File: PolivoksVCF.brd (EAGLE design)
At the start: 39.4 x 97.5 mm, 42 parts, among them IC1 TL072P, IC2 LM4250P, IC3 LM4250P

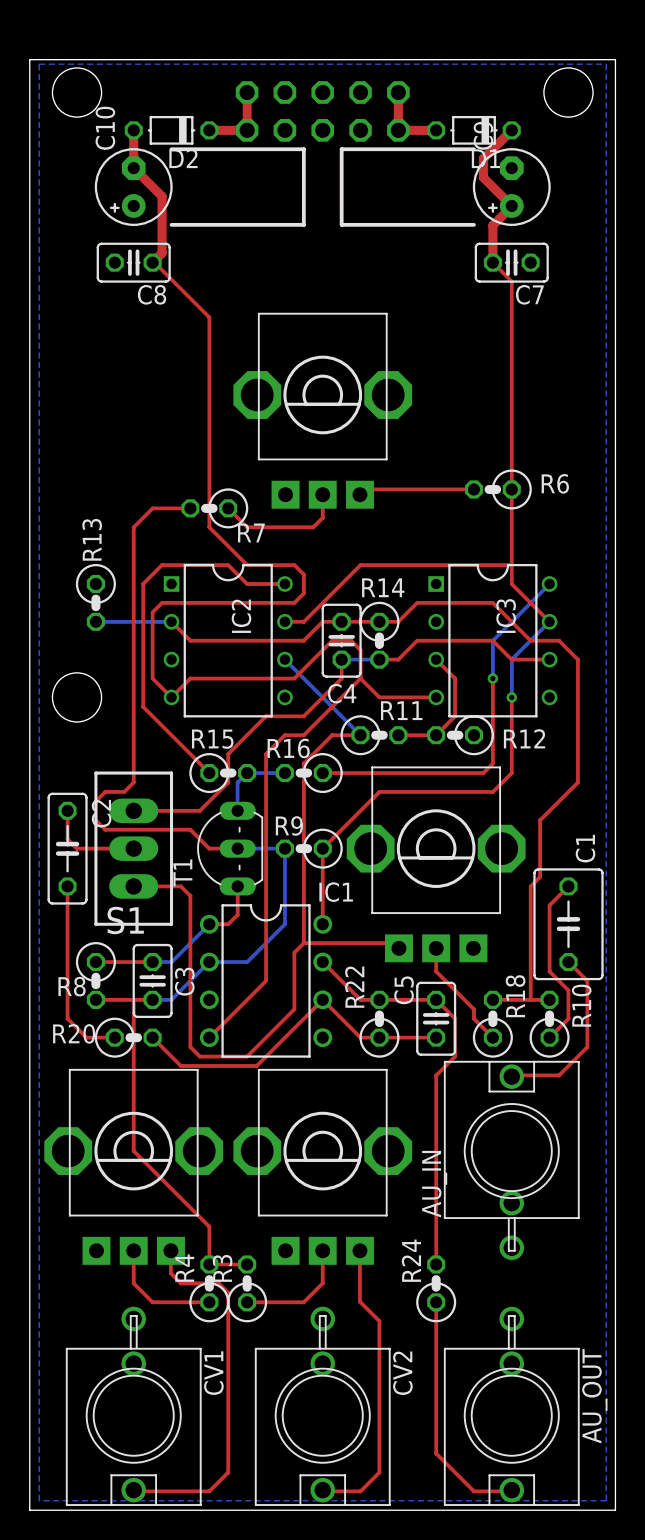
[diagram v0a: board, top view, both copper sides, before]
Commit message: Added labels to filter pcb. Added panel file.
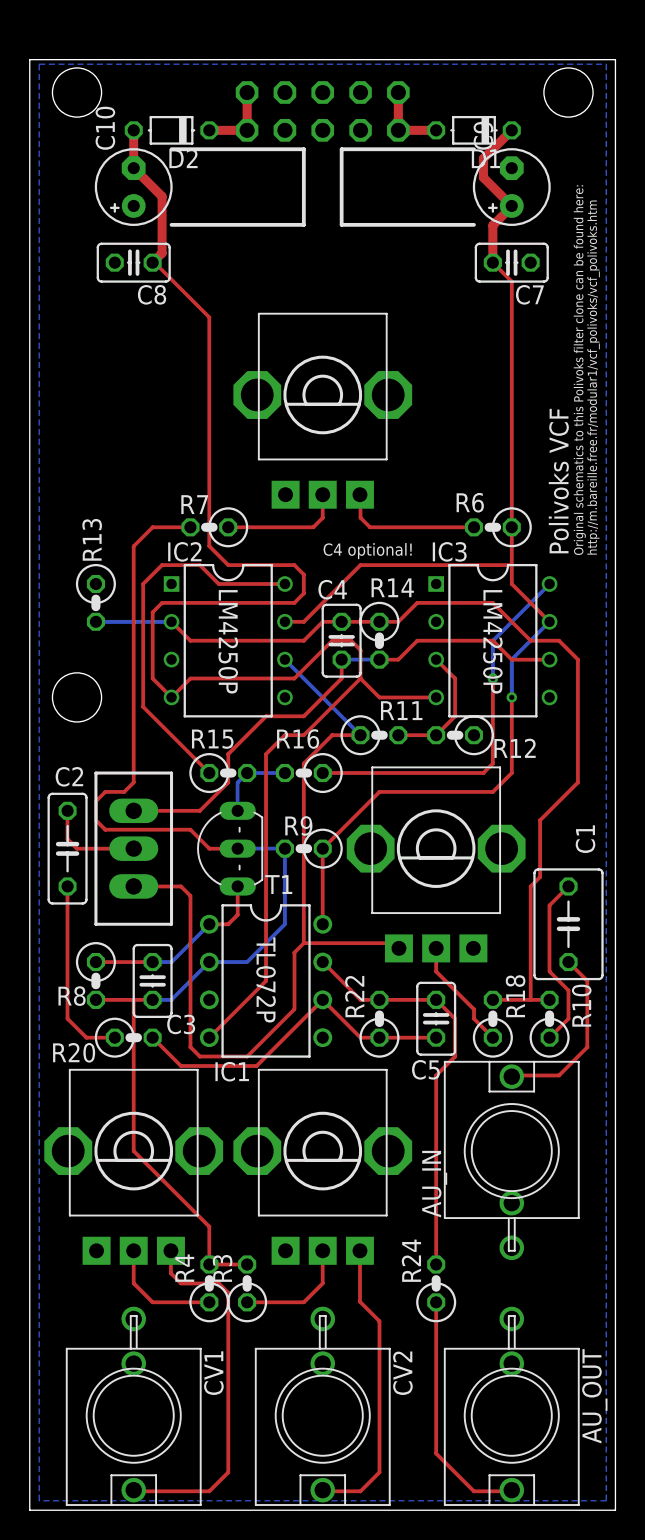
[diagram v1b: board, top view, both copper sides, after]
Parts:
- moved R6 2.54 mm to (31.8, 67.3)
- moved R7 1.27 mm to (12.7, 67.3)
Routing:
- net N$3: track 7.80 -> 9.45 mm
- net N$7: track 81.6 -> 80.4 mm
- net -12V: track 106.3 -> 107.1 mm
- net N$4: track 8.69 -> 8.17 mm
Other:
- board text added: "C4 optional!"
- board text added: "Original schematics to this Polivoks filter clone can be found here: http://m.bareille.free.fr/modular1/vcf_polivoks/vcf_polivoks.htm"
- board text added: "Polivoks VCF"

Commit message: Added value to T1 so it shows up on schematic.
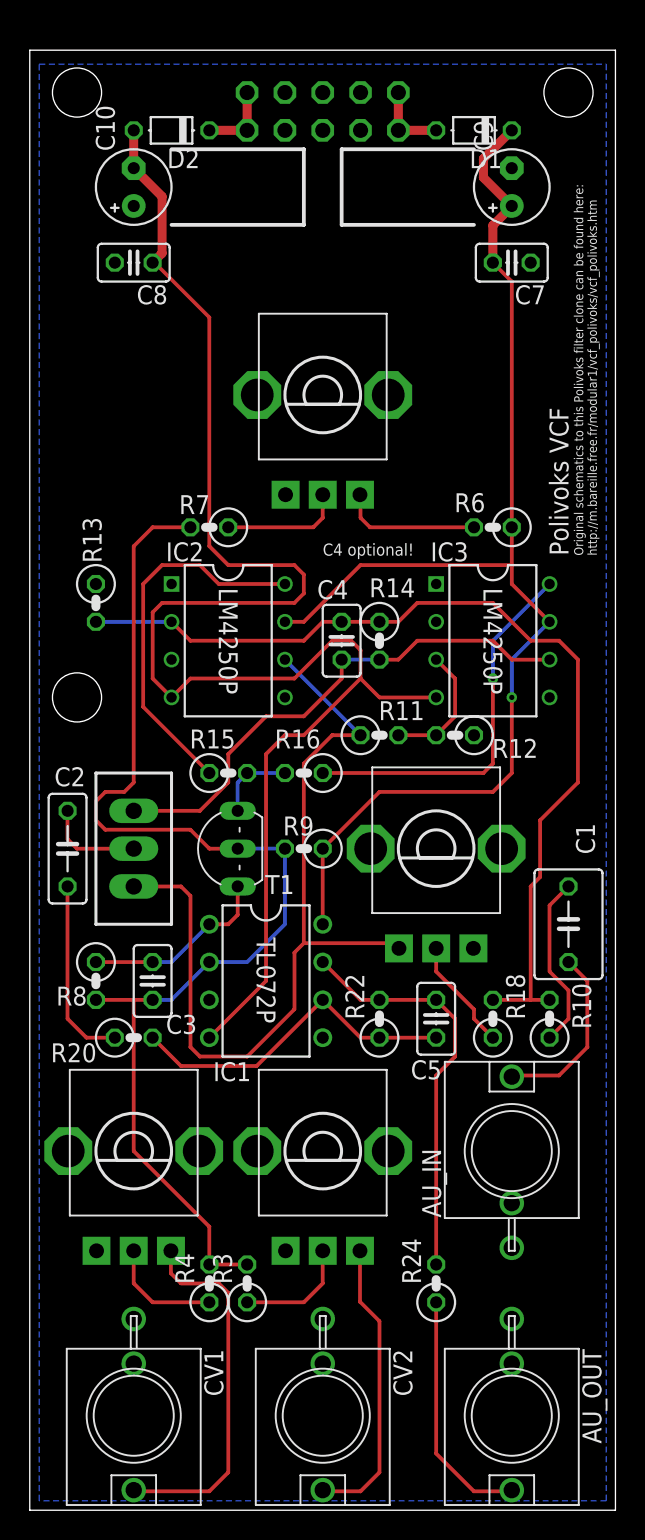
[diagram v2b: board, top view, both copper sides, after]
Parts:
- T1: value (none) -> 2N3904
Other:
- board size 39.4 x 97.5 mm -> 39.4 x 98.1 mm
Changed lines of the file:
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@@
 <plain>
 <wire x1="0.635" y1="1.27" x2="39.985" y2="1.27" width="0" layer="20"/>
-<wire x1="39.985" y1="1.27" x2="39.985" y2="98.73" width="0" layer="20"/>
-<wire x1="39.985" y1="98.73" x2="0.635" y2="98.73" width="0" layer="20"/>
-<wire x1="0.635" y1="98.73" x2="0.635" y2="1.27" width="0" layer="20"/>
+<wire x1="39.985" y1="1.27" x2="39.985" y2="99.365" width="0" layer="20"/>
+<wire x1="39.985" y1="99.365" x2="0.635" y2="99.365" width="0" layer="20"/>
+<wire x1="0.635" y1="99.365" x2="0.635" y2="1.27" width="0" layer="20"/>
 <hole x="3.81" y="55.88" drill="3.3"/>
 <hole x="3.81" y="96.52" drill="3.3"/>
@@
 <element name="AU_IN" library="thonkiconn" package="WQP-PJ301M-12_JACK" value="WQP-PJ301M-12_JACK" x="33.02" y="25.4"/>
 <element name="AU_OUT" library="thonkiconn" package="WQP-PJ301M-12_JACK" value="WQP-PJ301M-12_JACK" x="33.02" y="7.62" rot="R180"/>
-<element name="T1" library="transistor-neu-to92" package="TO92-EBC" value="" x="13.335" y="45.72" smashed="yes" rot="R90">
+<element name="T1" library="transistor-neu-to92" package="TO92-EBC" value="2N3904" x="13.335" y="45.72" smashed="yes" rot="R90">
 <attribute name="NAME" x="18.415" y="43.942" size="1.27" layer="25" ratio="10" rot="R180"/>
 <attribute name="VALUE" x="17.907" y="43.18" size="1.27" layer="27" ratio="10" rot="R90"/>
